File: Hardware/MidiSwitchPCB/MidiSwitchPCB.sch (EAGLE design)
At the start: 75 parts, among them IC3 74LVC2G04GW,125, J1 694108106102, Q1 BSS123, Q2 BSS123, Q3 BSS123, Q4 BSS123, Q5 BSS123, Q6 BSS123, Q7 BSS123, Q8 BSS123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

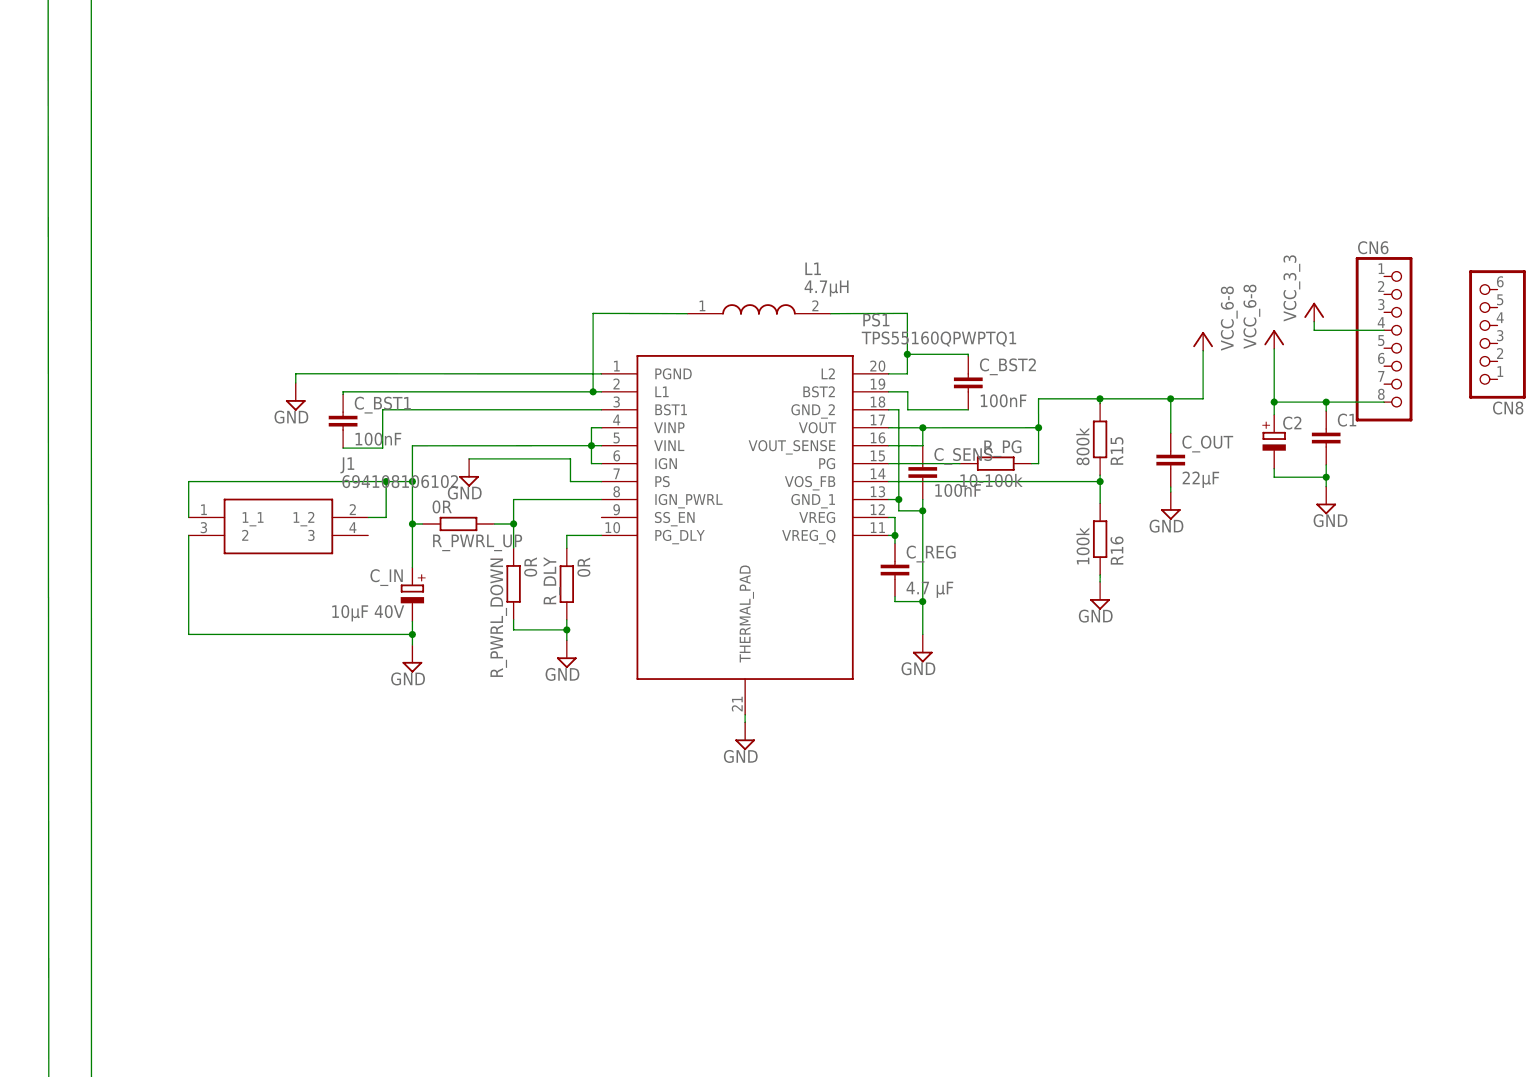
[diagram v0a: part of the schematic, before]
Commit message: Finished device placement and added a fuse as well as an ESD diode
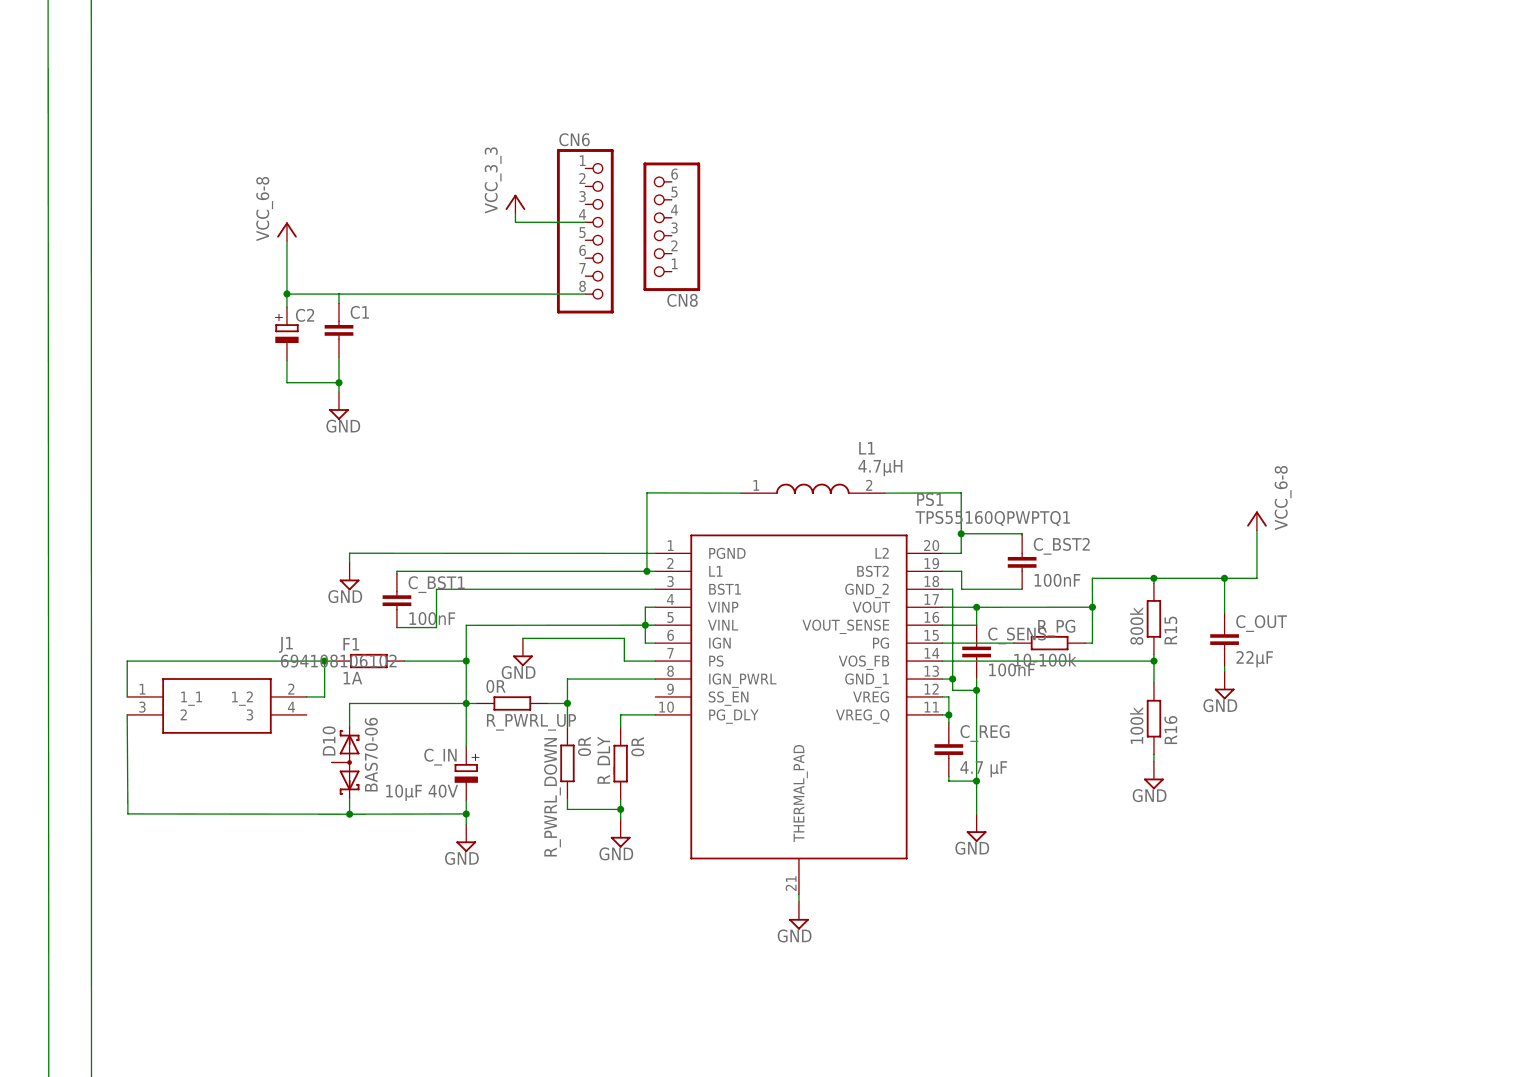
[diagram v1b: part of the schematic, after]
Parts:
- added D10: BAS70-06, diode:BAS70-06
- added F1: 1A, rcl:R-EU_R0603
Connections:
- new net N$50: F1.1, J1.1_1
- net GND: now also D10.K1
- net N$67: now also D10.K2, F1.2; no longer J1.1_1
- net VCC: now also C1.1, C2.+, CN6.8
- net VCC_6-8: no longer C1.1, C2.+, CN6.8
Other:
- moved on the sheet: C1, C2, CN6, CN8, C_BST1, C_BST2, C_IN, C_OUT, C_REG, C_SENS, J1, L1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

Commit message: started routing
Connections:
- net N$50 renamed VIN
- net N$67 renamed VIN_FUSED
- removed net VCC: C1.1, C2.+, CN6.4, CN6.8
- net VCC_3_3: now also CN6.4
- net VCC_6-8: now also C1.1, C2.+, CN6.8
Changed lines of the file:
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@@
 <setting verticaltext="up"/>
 </settings>
-<grid distance="0.01" unitdist="mm" unit="mm" style="lines" multiple="1" display="yes" altdistance="0.01" altunitdist="mm" altunit="mm"/>
+<grid distance="0.1" unitdist="inch" unit="inch" style="lines" multiple="1" display="no" altdistance="0.01" altunitdist="inch" altunit="inch"/>
 <layers>
 <layer number="1" name="Top" color="4" fill="1" visible="no" active="no"/>
@@
 </variantdefs>
 <classes>
-<class number="0" name="default" width="0" drill="0">
+<class number="0" name="default" width="0.4064" drill="1.016">
+<clearance class="0" value="0.4064"/>
+</class>
+<class number="1" name="Power" width="1.016" drill="1.016">
+<clearance class="1" value="0.4064"/>
+</class>
+<class number="2" name="Signal" width="0.4064" drill="0.6096">
+<clearance class="2" value="0.4064"/>
 </class>
 </classes>
@@
 </segment>
 </net>
-<net name="GND" class="0">
+<net name="GND" class="2">
 <segment>
 <wire x1="72.64" y1="78.46" x2="72.64" y2="75.21" width="0.1524" layer="91"/>
@@
 </segment>
 </net>
-<net name="N$51" class="0">
+<net name="N$51" class="1">
 <segment>
 <pinref part="PS1" gate="G$1" pin="L2"/>
@@
 </segment>
 </net>
-<net name="N$55" class="0">
+<net name="N$55" class="1">
 <segment>
 <pinref part="L1" gate="G$1" pin="1"/>
@@
 <junction x="39.46" y="56.42"/>
 </segment>
-</net>
-<net name="VCC_6-8" class="0">
+<segment>
+<pinref part="CN6" gate="A" pin="4"/>
+<pinref part="VCC_3_1" gate="VCC" pin="VCC"/>
+<wire x1="353.31" y1="90.03" x2="343.42" y2="90.03" width="0.1524" layer="91"/>
+<wire x1="343.42" y1="90.03" x2="343.42" y2="91.26" width="0.1524" layer="91"/>
+</segment>
+</net>
+<net name="VCC_6-8" class="1">
 <segment>
 <pinref part="PS1" gate="G$1" pin="VOUT_SENSE"/>
@@
 <junction x="228.6" y="-75.1"/>
 </segment>
-</net>
-<net name="N$1" class="0">
-<segment>
-<pinref part="IC3" gate="G$1" pin="2Y"/>
-<wire x1="54.1" y1="53.64" x2="53.19" y2="53.64" width="0.1524" layer="91"/>
-<wire x1="53.19" y1="53.64" x2="53.19" y2="58.38" width="0.1524" layer="91"/>
-<wire x1="53.19" y1="58.38" x2="85.02" y2="58.38" width="0.1524" layer="91"/>
-<wire x1="85.02" y1="58.38" x2="85.02" y2="48.56" width="0.1524" layer="91"/>
-<pinref part="IC3" gate="G$1" pin="1A"/>
-<wire x1="85.02" y1="48.56" x2="79.5" y2="48.56" width="0.1524" layer="91"/>
-</segment>
-</net>
-<net name="VCC" class="0">
-<segment>
-<pinref part="CN6" gate="A" pin="4"/>
-<pinref part="VCC_3_1" gate="VCC" pin="VCC"/>
-<wire x1="353.31" y1="90.03" x2="343.42" y2="90.03" width="0.1524" layer="91"/>
-<wire x1="343.42" y1="90.03" x2="343.42" y2="91.26" width="0.1524" layer="91"/>
-</segment>
 <segment>
 <pinref part="P+11" gate="VCC" pin="VCC"/>
@@
 </segment>
 </net>
+<net name="N$1" class="0">
+<segment>
+<pinref part="IC3" gate="G$1" pin="2Y"/>
+<wire x1="54.1" y1="53.64" x2="53.19" y2="53.64" width="0.1524" layer="91"/>
+<wire x1="53.19" y1="53.64" x2="53.19" y2="58.38" width="0.1524" layer="91"/>
+<wire x1="53.19" y1="58.38" x2="85.02" y2="58.38" width="0.1524" layer="91"/>
+<wire x1="85.02" y1="58.38" x2="85.02" y2="48.56" width="0.1524" layer="91"/>
+<pinref part="IC3" gate="G$1" pin="1A"/>
+<wire x1="85.02" y1="48.56" x2="79.5" y2="48.56" width="0.1524" layer="91"/>
+</segment>
+</net>
 <net name="N$58" class="0">
 <segment>
@@
 </segment>
 </net>
-<net name="N$67" class="0">
+<net name="VIN_FUSED" class="1">
 <segment>
 <pinref part="PS1" gate="G$1" pin="VINP"/>
@@
 </segment>
 </net>
-<net name="N$50" class="0">
+<net name="VIN" class="1">
 <segment>
 <wire x1="316.42" y1="22.86" x2="313.89" y2="22.86" width="0.1524" layer="91"/>

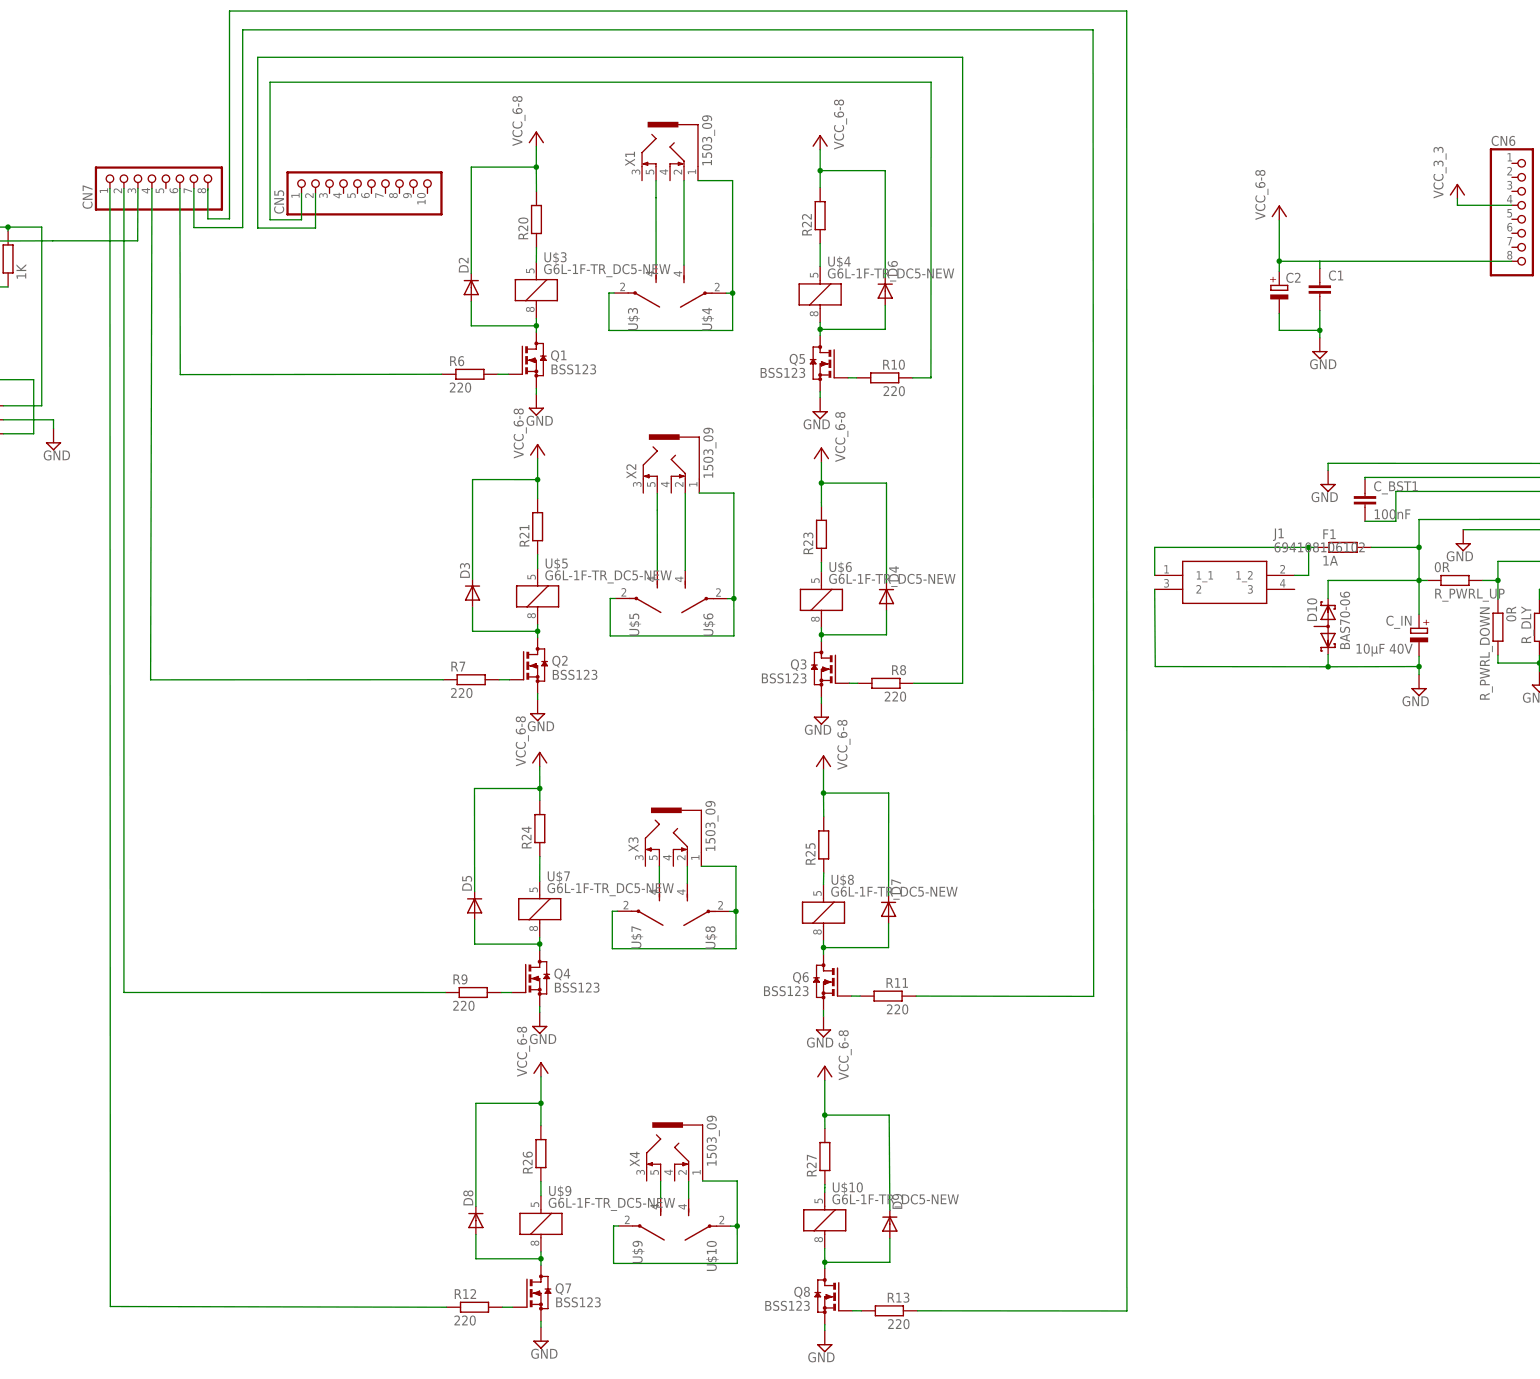
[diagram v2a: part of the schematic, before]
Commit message: continued layout design. The pinheaders are unfortunately connected on the wrong pcb side.
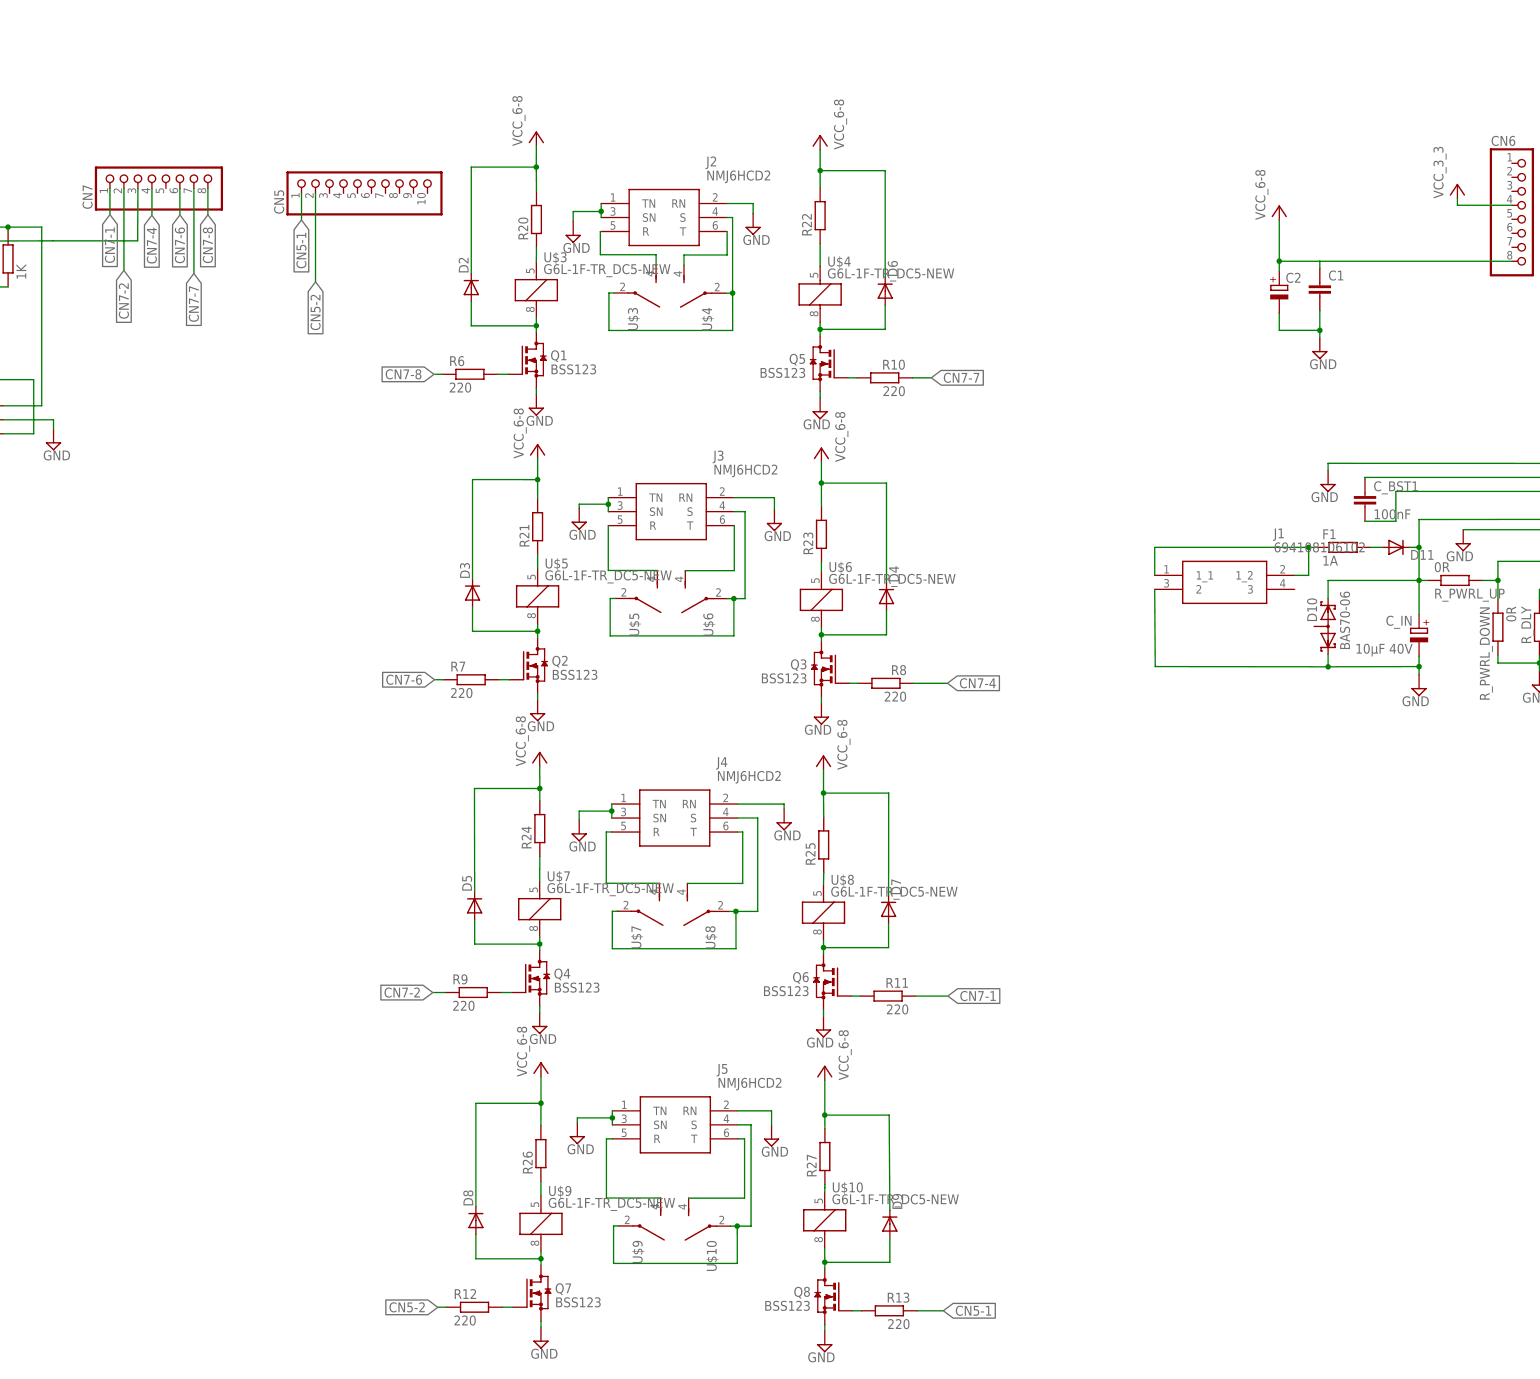
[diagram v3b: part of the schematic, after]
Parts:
- removed X1, X2, X3, X4: 1503_09, con-lumberg:1503_09
- added D11: (no value), diode:DIODE-DO-214AC
- added J2, J3, J4, J5: NMJ6HCD2, NMJ6HCD2:NMJ6HCD2
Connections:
- net N$28 renamed CN7-2
- removed net N$18: CN7.4, R7.1
- removed net N$31: CN7.6, R6.1
- removed net N$40: CN7.1, R12.1
- removed net N$42: U$10G$2.S, X4.2
- removed net N$44: CN7.8, R13.1
- removed net N$45: CN5.2, R8.1
- removed net N$46: CN7.7, R11.1
- removed net N$47: CN5.1, R10.1
- new net CN5-1: CN5.1, R13.1
- new net CN5-2: CN5.2, R12.1
- new net CN7-1: CN7.1, R11.1
- new net CN7-4: CN7.4, R8.1
- new net CN7-6: CN7.6, R7.1
- new net CN7-7: CN7.7, R10.1
- new net CN7-8: CN7.8, R6.1
- new net N$50: J5.T, U$10G$2.S
- new net N$66: D11.A, F1.2
- net GND: now also J2.RN, J2.SN, J2.TN, J3.RN, J3.SN, J3.TN, J4.RN, J4.SN, J4.TN, J5.RN, J5.SN, J5.TN
- net N$19: now also J3.R; no longer X2.5
- net N$22: now also J3.T; no longer X2.2
- net N$23: now also J3.S; no longer X2.1
- net N$29: now also J4.T, U$8G$2.S; no longer U$7G$2.S, X3.5
- net N$30: now also J4.R, U$7G$2.S; no longer U$8G$2.S, X3.2
- net N$32: now also J4.S; no longer X3.1
- net N$36: now also J2.R; no longer X1.5
- net N$37: now also J2.T; no longer X1.2
- net N$38: now also J2.S; no longer X1.1
- net N$41: now also J5.R; no longer X4.5
- net N$43: now also J5.S; no longer X4.1
- net VIN_FUSED: now also D11.C; no longer F1.2
